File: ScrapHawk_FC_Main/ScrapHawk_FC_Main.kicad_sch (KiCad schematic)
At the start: 46 parts, among them J1 USB_C_Receptacle_USB2.0_16P, J2 Conn_01x06, J3 Conn_01x06, U1 RP2040, U2 W25Q128JVS, U3 AMS1117CD-3.3, U4 LSM6DS3TR, U5 TPS562200, Y1 12M

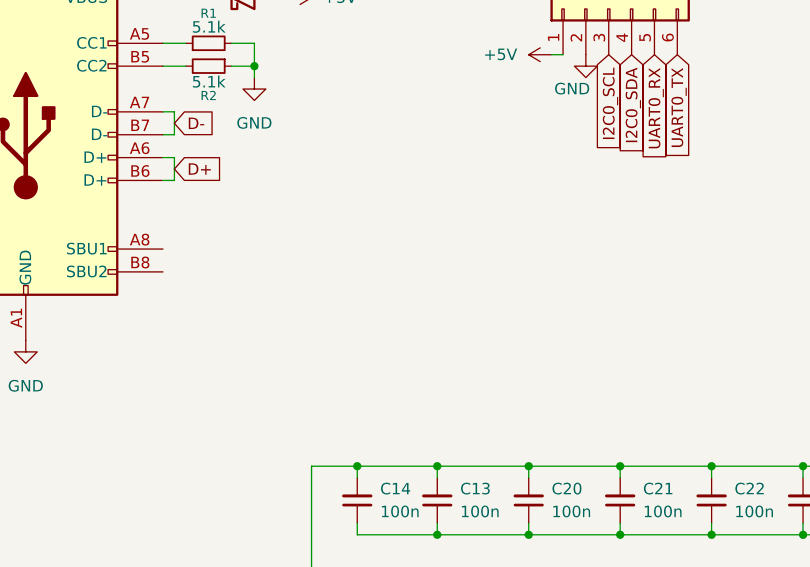
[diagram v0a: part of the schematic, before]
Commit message: update decoupling capacitor battery
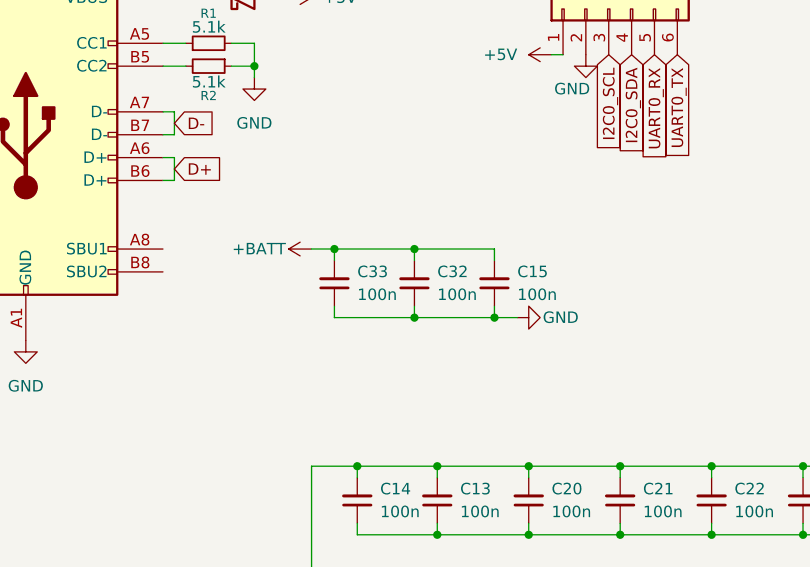
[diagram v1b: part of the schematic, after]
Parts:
- added C15, C32, C33: 100n, Capacitor_SMD:C_1206_3216Metric, symbol Device:C_Small
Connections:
- net +BATT: now also C15.2, C32.2, C33.2
- net GND: now also C15.1, C32.1, C33.1
